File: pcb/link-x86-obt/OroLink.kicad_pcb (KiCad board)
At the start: 4 copper layers, 114.9 x 65.4 mm, 168 parts, among them IC1 STM32F479VGT6, IC10 ENC28J60-I_SO, IC11 PMV20ENR, IC12 PMV20ENR, IC13 PMV20ENR, IC14 SN75C3232EPWR, IC15 PMV20ENR, IC16 PMV20ENR, IC17 IS31FL3218-GRLS2, IC2 PMV20ENR, IC3 PMV20ENR, IC4 TPS6734ID, IC5 PMV20ENR, IC6 PMV20ENR, IC7 ENC28J60-I_SO, IC8 PMV20ENR, IC9 PMV20ENR, J1 67996-408HLF, J2 DF63-5P-3.96DSA, J3 67996-408HLF, J4 3-2328724-1, J5 74990101241, J6 74990101241, J7 2P SHORT, J8 STLINK-V3MINIE, Q1 PMV20ENR, Q2 PMV20ENR, Q3 PMV20ENR, X1 7P-26.000MBP-T, Y1 25MHz, Y2 25MHz

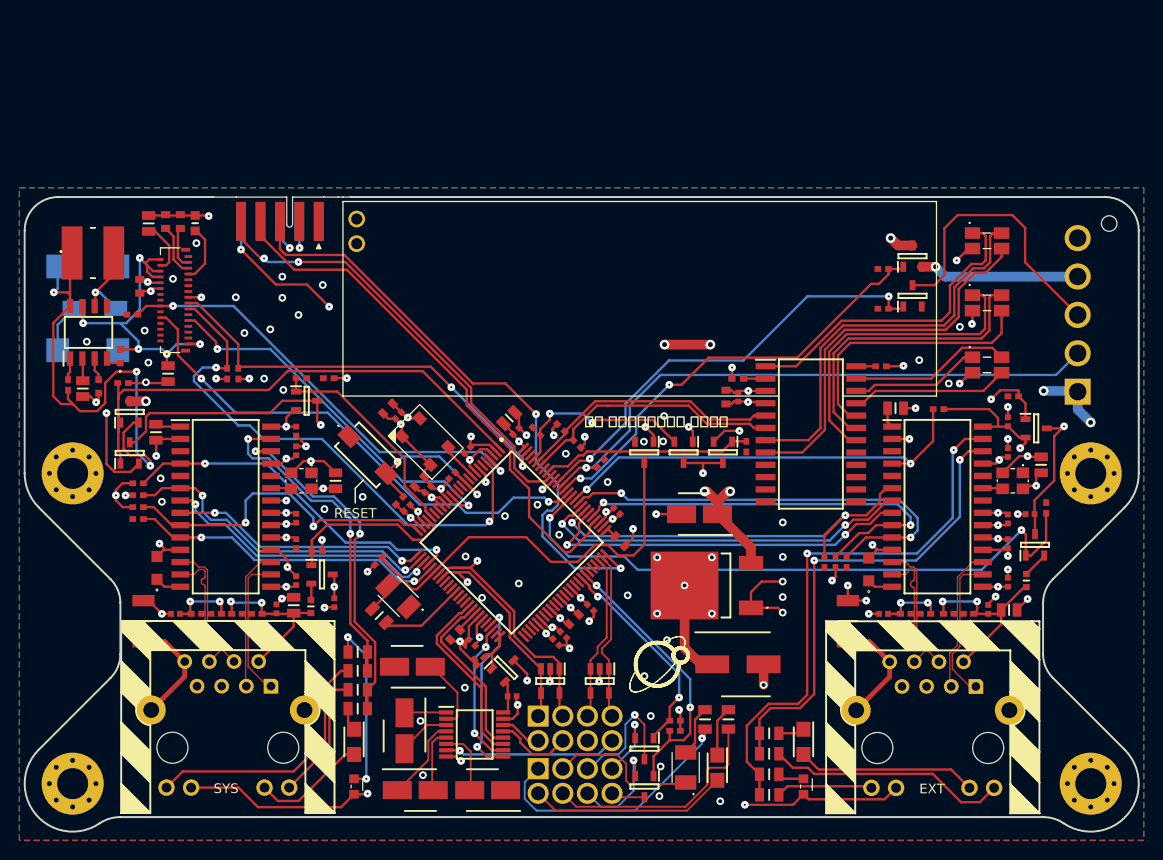
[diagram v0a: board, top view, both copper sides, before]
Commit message: add P-channel mosfet to 5VSB line
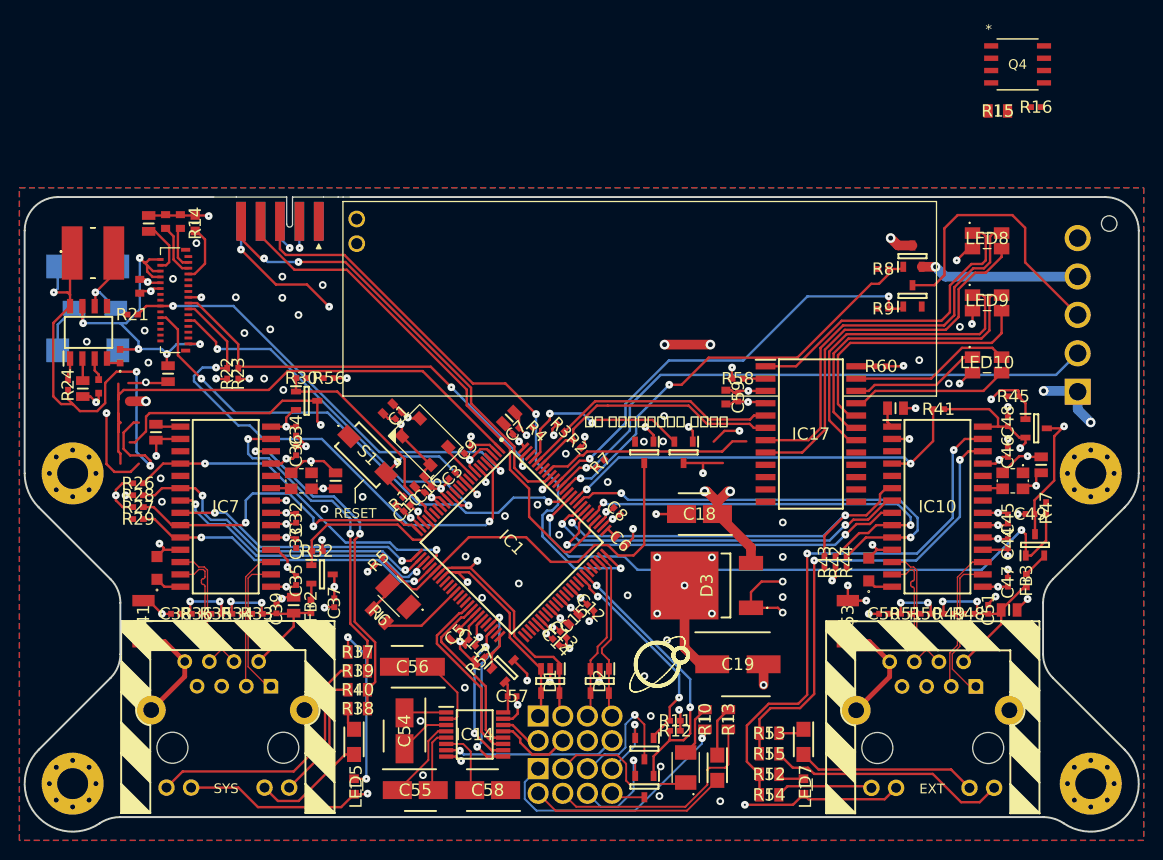
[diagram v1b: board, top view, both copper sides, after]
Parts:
- removed IC16, IC3, IC5: PMV20ENR, SamacSys_Parts:SOT95P230X110-3N
- removed R25, R59: 10k, SamacSys_Parts:RESC1005X40N
- added Q4: SI4403DDY-T1-GE3, Oro:SO-8_MS-012_VIS, F.Cu at (193.3, 34.9)
- added R15: 1k, SamacSys_Parts:RESC2012X60N, F.Cu at (191.2, 39.7)
- added R16: 10k, SamacSys_Parts:RESC1005X40N, F.Cu at (195.2, 39.3)
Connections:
- C23 pad 2: /OLED Socket/VCC_EN -> +3V3
- C28 pad 1: Net-(IC4-VCC) -> +5V
- C59 pad 1: /Indicator Lights/EN_3V3 -> +3V3
- C60 pad 2: /Indicator Lights/EN_3V3 -> +3V3
- FB1 pad 1: Net-(IC4-VCC) -> +5V
- IC17 pad 24: Net-(IC17-~{SDB}) -> /Indicator Lights/EN
- IC17 pad 3: /Indicator Lights/EN_3V3 -> +3V3
- IC2 pad 1: /Power Supply/PW_SB -> Net-(IC2-Pad1)
- IC2 pad 2: /Power Supply/5VSB_ON -> GND
- IC2 pad 3: +5V -> Net-(IC2-Pad3)
- IC4 pad 1: Net-(IC4-EN) -> /OLED Socket/ENABLE
- IC4 pad 8: Net-(IC4-VCC) -> +5V
- J4 pad 12: /OLED Socket/VCC_EN -> +3V3
- J4 pad 15: /OLED Socket/VCC_EN -> +3V3
- LED10 pad 2: /Indicator Lights/EN_3V3 -> +3V3
- LED8 pad 2: /Indicator Lights/EN_3V3 -> +3V3
- LED9 pad 2: /Indicator Lights/EN_3V3 -> +3V3
- R23 pad 1: /OLED Socket/VCC_EN -> +3V3
- R24 pad 1: Net-(IC4-EN) -> /OLED Socket/ENABLE
- R24 pad 2: Net-(IC4-VCC) -> GND
- R60 pad 1: /Indicator Lights/EN_3V3 -> /Indicator Lights/EN
- R60 pad 2: Net-(IC17-~{SDB}) -> GND
- R8 pad 1: /Power Supply/PW_SB -> +5V
- R8 pad 2: GND -> Net-(IC2-Pad3)
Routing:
- net +3V3: track 116.3 -> 138.8 mm, vias 28 -> 36
- net /OLED Socket/VCC_EN: track 13.8 -> 0.00 mm, vias 4 -> 0
- net /Indicator Lights/EN_3V3: track 13.6 -> 3.12 mm, vias 6 -> 1
- net /OLED Socket/ENABLE: track 54.5 -> 56.7 mm
- net Net-(IC4-EN): track 2.26 -> 0.00 mm
- net /Indicator Lights/EN: track 21.8 -> 23.6 mm, vias 0 -> 1
- net Net-(IC4-VCC): vias 3 -> 0
- net GND: vias 101 -> 104
- added copper zone on In2.Cu, net /Indicator Lights/EN
- removed copper zone on In2.Cu, net /Indicator Lights/EN_3V3
- removed copper zone on In2.Cu, net /OLED Socket/VCC_EN

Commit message: omit ethernet enable mosfets in lieu of reset mosfet
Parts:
- removed IC6, IC9: PMV20ENR, SamacSys_Parts:SOT95P230X110-3N
- removed R30, R45: 10k, SamacSys_Parts:RESC1005X40N
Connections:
- C31 pad 1: /System Ethernet/VCC_EN -> +3V3
- C43 pad 1: /External Ethernet/VCC_EN -> +3V3
- IC1 pad 21: /Microcontroller/SYSETH_EN -> unconnected-(IC1-PA2-Pad21)
- IC1 pad 91: /External Ethernet/EN -> unconnected-(IC1-PD7-Pad91)
- J5 pad 11: /System Ethernet/VCC_EN -> +3V3
- J6 pad 11: /External Ethernet/VCC_EN -> +3V3
- R26 pad 2: /System Ethernet/VCC_EN -> +3V3
- R27 pad 2: /System Ethernet/VCC_EN -> +3V3
- R41 pad 2: /External Ethernet/VCC_EN -> +3V3
- R42 pad 2: /External Ethernet/VCC_EN -> +3V3
- Y1 pad 4: /System Ethernet/VCC_EN -> +3V3
- Y2 pad 4: /External Ethernet/VCC_EN -> +3V3
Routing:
- net +5V: track 136.5 -> 76.8 mm, vias 4 -> 2
- net /External Ethernet/EN: track 59.5 -> 0.00 mm, vias 2 -> 0
- net /OLED Socket/ENABLE: track 56.7 -> 2.26 mm
- net Net-(IC4-VCC): track 51.4 -> 0.00 mm
- net /Power Supply/PW_SB: track 45.7 -> 0.00 mm, vias 2 -> 0
- net /System Ethernet/VCC_EN: track 42.0 -> 14.2 mm, vias 8 -> 6
- net +3V3: track 138.8 -> 112.2 mm, vias 36 -> 38
- net /Microcontroller/SYSETH_EN: track 22.6 -> 0.00 mm
- net /Indicator Lights/EN: track 23.6 -> 1.79 mm
- net /External Ethernet/VCC_EN: track 43.8 -> 23.0 mm, vias 8 -> 6
- net /Power Supply/5VSB_ON: track 16.4 -> 0.00 mm, vias 1 -> 0
- net /Indicator Lights/EN_3V3: track 3.12 -> 0.00 mm, vias 1 -> 0
- net Net-(IC17-~{SDB}): track 2.01 -> 0.00 mm
- net GND: track 186.5 -> 184.8 mm, vias 104 -> 101

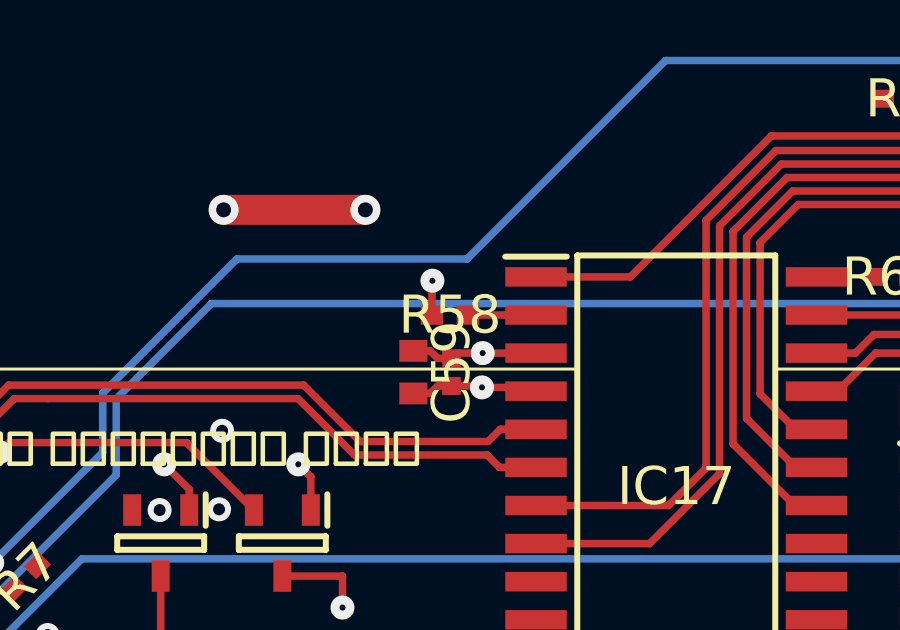
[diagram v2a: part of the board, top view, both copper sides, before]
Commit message: increase current limiting resistor for indicator lights
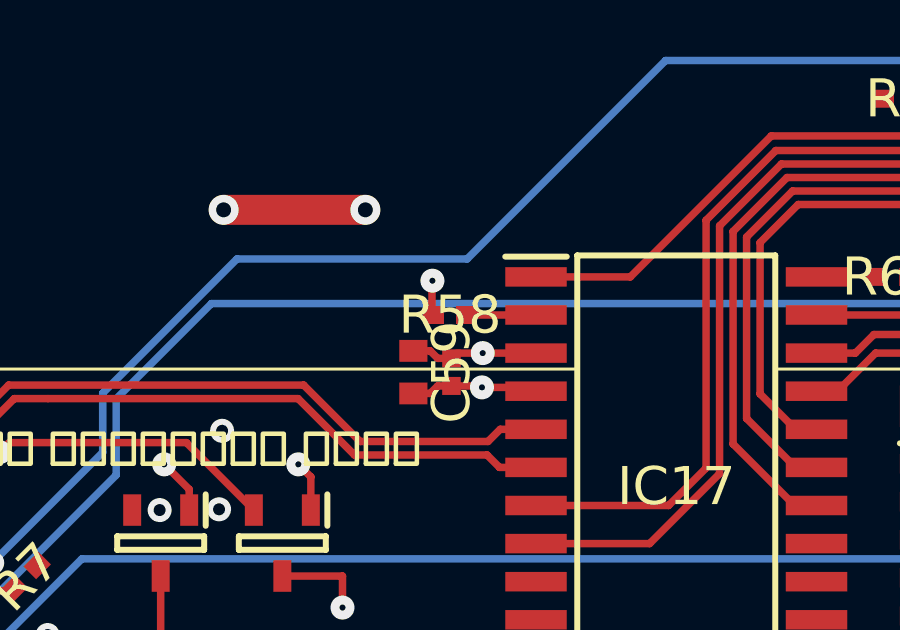
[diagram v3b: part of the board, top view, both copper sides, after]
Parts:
- R58: value 5.6K -> 10k; footprint SamacSys_Parts:RESC1105X40N -> SamacSys_Parts:RESC1005X40N
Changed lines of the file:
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@@
 		)
 	)
-	(footprint "SamacSys_Parts:RESC1105X40N"
+	(footprint "SamacSys_Parts:RESC1005X40N"
 		(layer "F.Cu")
 		(at 164.416 67.31)
-		(descr "0402")
+		(descr "1E(0402)")
 		(tags "Resistor")
 		(property "Reference" "R58"
@@
 			)
 		)
-		(property "Value" "5.6K"
+		(property "Value" "10k"
 			(at 0 0 0)
 			(layer "F.SilkS")
@@
 			)
 		)
-		(property "Footprint" "RESC1105X40N"
-			(at 0 0 0)
-			(unlocked yes)
-			(layer "F.Fab")
-			(hide yes)
-			(effects
-				(font
-					(size 1.27 1.27)
-				)
-			)
-		)
-		(property "Datasheet" "https://www.mouser.de/datasheet/2/418/8/ENG_DS_9_1773463_9_B-1358566.pdf"
-			(at 0 0 0)
-			(unlocked yes)
-			(layer "F.Fab")
-			(hide yes)
-			(effects
-				(font
-					(size 1.27 1.27)
-				)
-			)
-		)
-		(property "Description" "5.6k 0402 Thick Film Resistor +/-1% 0.12W CRGP0402F5K6"
-			(at 0 0 0)
-			(unlocked yes)
-			(layer "F.Fab")
-			(hide yes)
-			(effects
-				(font
-					(size 1.27 1.27)
-				)
-			)
-		)
-		(property "Arrow Part Number" ""
-			(at 0 0 0)
-			(layer "F.Fab")
-			(hide yes)
-			(effects
-				(font
-					(size 1 1)
-					(thickness 0.15)
-				)
-			)
-		)
-		(property "Arrow Price/Stock" ""
+		(property "Footprint" "RESC1005X40N"
+			(at 0 0 0)
+			(unlocked yes)
+			(layer "F.Fab")
+			(hide yes)
+			(effects
+				(font
+					(size 1.27 1.27)
+				)
+			)
+		)
+		(property "Datasheet" "http://www.koaspeer.com/catimages/Products/RK73-RT/RK73-RT.pdf"
+			(at 0 0 0)
+			(unlocked yes)
+			(layer "F.Fab")
+			(hide yes)
+			(effects
+				(font
+					(size 1.27 1.27)
+				)
+			)
+		)
+		(property "Description" "Resistor,ThickFilm1005,0.063W,10kohm"
+			(at 0 0 0)
+			(unlocked yes)
+			(layer "F.Fab")
+			(hide yes)
+			(effects
+				(font
+					(size 1.27 1.27)
+				)
+			)
+		)
+		(property "Arrow Part Number" "RK73H1ETTP1002F"
+			(at 0 0 0)
+			(layer "F.Fab")
+			(hide yes)
+			(effects
+				(font
+					(size 1 1)
+					(thickness 0.15)
+				)
+			)
+		)
+		(property "Arrow Price/Stock" "https://www.arrow.com/en/products/rk73h1ettp1002f/koa-speer-electronics?region=nac"
 			(at 0 0 0)
 			(layer "F.Fab")
@@
 			)
 		)
-		(property "Manufacturer_Name" "TE Connectivity"
-			(at 0 0 0)
-			(layer "F.Fab")
-			(hide yes)
-			(effects
-				(font
-					(size 1 1)
-					(thickness 0.15)
-				)
-			)
-		)
-		(property "Manufacturer_Part_Number" "CRGP0402F5K6"
-			(at 0 0 0)
-			(layer "F.Fab")
-			(hide yes)
-			(effects
-				(font
-					(size 1 1)
-					(thickness 0.15)
-				)
-			)
-		)
-		(property "Mouser Part Number" "279-CRGP0402F5K6"
-			(at 0 0 0)
-			(layer "F.Fab")
-			(hide yes)
-			(effects
-				(font
-					(size 1 1)
-					(thickness 0.15)
-				)
-			)
-		)
-		(property "Mouser Price/Stock" "https://www.mouser.de/ProductDetail/TE-Connectivity-Holsworthy/CRGP0402F5K6?qs=wUXugUrL1qxVwNCmbd06hg%3D%3D"
-			(at 0 0 0)
+		(property "Manufacturer_Name" "KOA Speer"
+			(at 0 0 0)
+			(layer "F.Fab")
+			(hide yes)
+			(effects
+				(font
+					(size 1 1)
+					(thickness 0.15)
+				)
+			)
+		)
+		(property "Manufacturer_Part_Number" "RK73H1ETTP1002F"
+			(at 0 0 0)
+			(layer "F.Fab")
+			(hide yes)
+			(effects
+				(font
+					(size 1 1)
+					(thickness 0.15)
+				)
+			)
+		)
+		(property "Mouser Part Number" "660-RK73H1ETTP1002F"
+			(at 0 0 0)
+			(layer "F.Fab")
+			(hide yes)
+			(effects
+				(font
+					(size 1 1)
+					(thickness 0.15)
+				)
+			)
+		)
+		(property "Mouser Price/Stock" "https://www.mouser.co.uk/ProductDetail/KOA-Speer/RK73H1ETTP1002F?qs=uLfVlVfCHH2OZ4JTybrBPQ%3D%3D"
+			(at 0 0 0)
+			(layer "F.Fab")
+			(hide yes)
+			(effects
+				(font
+					(size 1 1)
+					(thickness 0.15)
+				)
+			)
+		)
+		(property "Mouser Testing Part Number" ""
+			(at 0 0 0)
+			(unlocked yes)
+			(layer "F.Fab")
+			(hide yes)
+			(effects
+				(font
+					(size 1 1)
+					(thickness 0.15)
+				)
+			)
+		)
+		(property "Mouser Testing Price/Stock" ""
+			(at 0 0 0)
+			(unlocked yes)
 			(layer "F.Fab")
 			(hide yes)
@@
 		(attr smd)
 		(fp_line
-			(start -1.225 -0.6)
-			(end 1.225 -0.6)
-			(stroke
-				(width 0.05)
-				(type solid)
-			)
-			(layer "F.CrtYd")
-		)
-		(fp_line
-			(start -1.225 0.6)
-			(end -1.225 -0.6)
-			(stroke
-				(width 0.05)
-				(type solid)
-			)
-			(layer "F.CrtYd")
-		)
-		(fp_line
-			(start 1.225 -0.6)
-			(end 1.225 0.6)
-			(stroke
-				(width 0.05)
-				(type solid)
-			)
-			(layer "F.CrtYd")
-		)
-		(fp_line
-			(start 1.225 0.6)
-			(end -1.225 0.6)
-			(stroke
-				(width 0.05)
-				(type solid)
-			)
-			(layer "F.CrtYd")
-		)
-		(fp_line
-			(start -0.55 -0.262)
-			(end 0.55 -0.262)
-			(stroke
-				(width 0.1)
-				(type solid)
-			)
-			(layer "F.Fab")
-		)
-		(fp_line
-			(start -0.55 0.262)
-			(end -0.55 -0.262)
-			(stroke
-				(width 0.1)
-				(type solid)
-			)
-			(layer "F.Fab")
-		)
-		(fp_line
-			(start 0.55 -0.262)
-			(end 0.55 0.262)
-			(stroke
-				(width 0.1)
-				(type solid)
-			)
-			(layer "F.Fab")
-		)
-		(fp_line
-			(start 0.55 0.262)
-			(end -0.55 0.262)
+			(start -1.15 -0.55)
+			(end 1.15 -0.55)
+			(stroke
+				(width 0.05)
+				(type solid)
+			)
+			(layer "F.CrtYd")
+		)
+		(fp_line
+			(start -1.15 0.55)
+			(end -1.15 -0.55)
+			(stroke
+				(width 0.05)
+				(type solid)
+			)
+			(layer "F.CrtYd")
+		)
+		(fp_line
+			(start 1.15 -0.55)
+			(end 1.15 0.55)
+			(stroke
+				(width 0.05)
+				(type solid)
+			)
+			(layer "F.CrtYd")
+		)
+		(fp_line
+			(start 1.15 0.55)
+			(end -1.15 0.55)
+			(stroke
+				(width 0.05)
+				(type solid)
+			)
+			(layer "F.CrtYd")
+		)
+		(fp_line
+			(start -0.512 -0.25)
+			(end 0.512 -0.25)
+			(stroke
+				(width 0.1)
+				(type solid)
+			)
+			(layer "F.Fab")
+		)
+		(fp_line
+			(start -0.512 0.25)
+			(end -0.512 -0.25)
+			(stroke
+				(width 0.1)
+				(type solid)
+			)
+			(layer "F.Fab")
+		)
+		(fp_line
+			(start 0.512 -0.25)
+			(end 0.512 0.25)
+			(stroke
+				(width 0.1)
+				(type solid)
+			)
+			(layer "F.Fab")
+		)
+		(fp_line
+			(start 0.512 0.25)
+			(end -0.512 0.25)
 			(stroke
 				(width 0.1)
@@
 		)
 		(pad "1" smd rect
-			(at -0.6 0 90)
-			(size 0.65 0.75)
+			(at -0.55 0 90)
+			(size 0.6 0.7)
 			(layers "F.Cu" "F.Paste" "F.Mask")
 			(net 1 "GND")
@@
 		)
 		(pad "2" smd rect
-			(at 0.6 0 90)
-			(size 0.65 0.75)
+			(at 0.55 0 90)
+			(size 0.6 0.7)
 			(layers "F.Cu" "F.Paste" "F.Mask")
 			(net 189 "Net-(IC17-R_EXT)")
 			(pintype "passive")
 		)
-		(model "O:\\KiCad Library\\SamacSys_Parts.3dshapes\\CRGP0402F5K6.stp"
+		(model "O:\\KiCad Library\\SamacSys_Parts.3dshapes\\RK73H1ETTP1002F.stp"
 			(offset
 				(xyz 0 0 0)

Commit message: add VBUS and ground headers
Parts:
- added D5: SS12, Oro Footprints:DIOM5227X250N, B.Cu at (176.8, 35.0)
- added J9: 67996-408HLF (2P CUT), Oro Footprints:HDRV8W89P254_2X4_1016X483X858P_2P, F.Cu at (174.8, 41.8)
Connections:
- IC1 pad 71: unconnected-(IC1-PA9-Pad71) -> /Microcontroller/USB_VBUS
